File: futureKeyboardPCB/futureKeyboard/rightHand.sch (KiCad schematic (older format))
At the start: 56 parts, among them J1 Conn_01x01, J17 Conn_01x15, J18 Conn_01x15, J2 Conn_01x02, J21 Conn_01x04, J22 Conn_01x04, J25 Conn_01x02, J3 Conn_01x01, J4 Conn_01x01, J5 Conn_01x04, J6 Conn_01x06, J7 Conn_01x06, J8 Conn_01x01, P1 CONN_01X02, P2 CONN_01X06, Q1 2SC1815, Q2 2SC1815, Q3 2SC1815, SW1 SW_SPDT, SW2 SW_Push, SW3 SW_Push, SW4 SW_Push, SW5 SW_Push, SW6 SW_Push, SW7 SW_Push, SW8 SW_Push, U1 AMS1117-1.5, U2 ESP32, U5 joystick

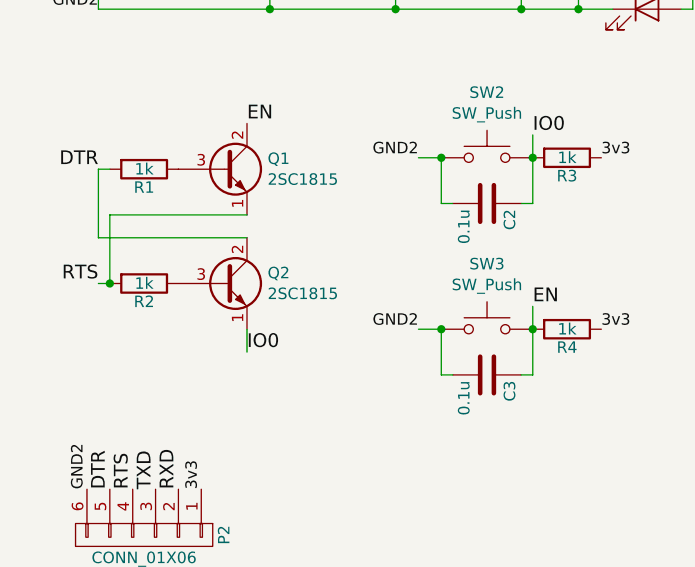
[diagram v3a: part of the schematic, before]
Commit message: complete placement electronic parts
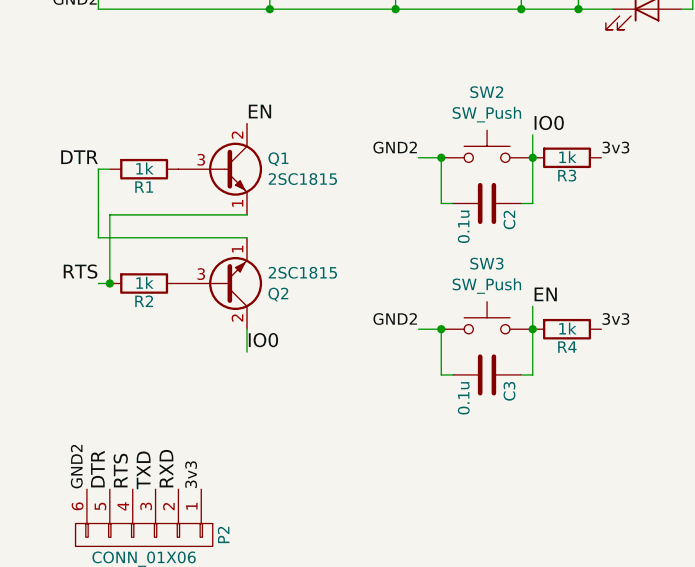
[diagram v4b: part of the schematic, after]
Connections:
- net DTR: now also Q2.1 (E); no longer Q2.2 (C)
- net IO0: now also Q2.2 (C); no longer Q2.1 (E)
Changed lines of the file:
@@
 F 3 "https://media.digikey.com/pdf/Data%20Sheets/Toshiba%20PDFs/2SC1815.pdf" H 1650 2650 50  0001 L CNN
 	1    1650 2650
-	1    0    0    -1
+	1    0    0    1
 $EndComp
 Text Label 1750 1950 0    60   ~ 0
